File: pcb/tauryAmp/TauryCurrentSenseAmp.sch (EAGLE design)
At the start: 20 parts, among them IC1 AD780R, U1 MAX4239, U2 MAX4239

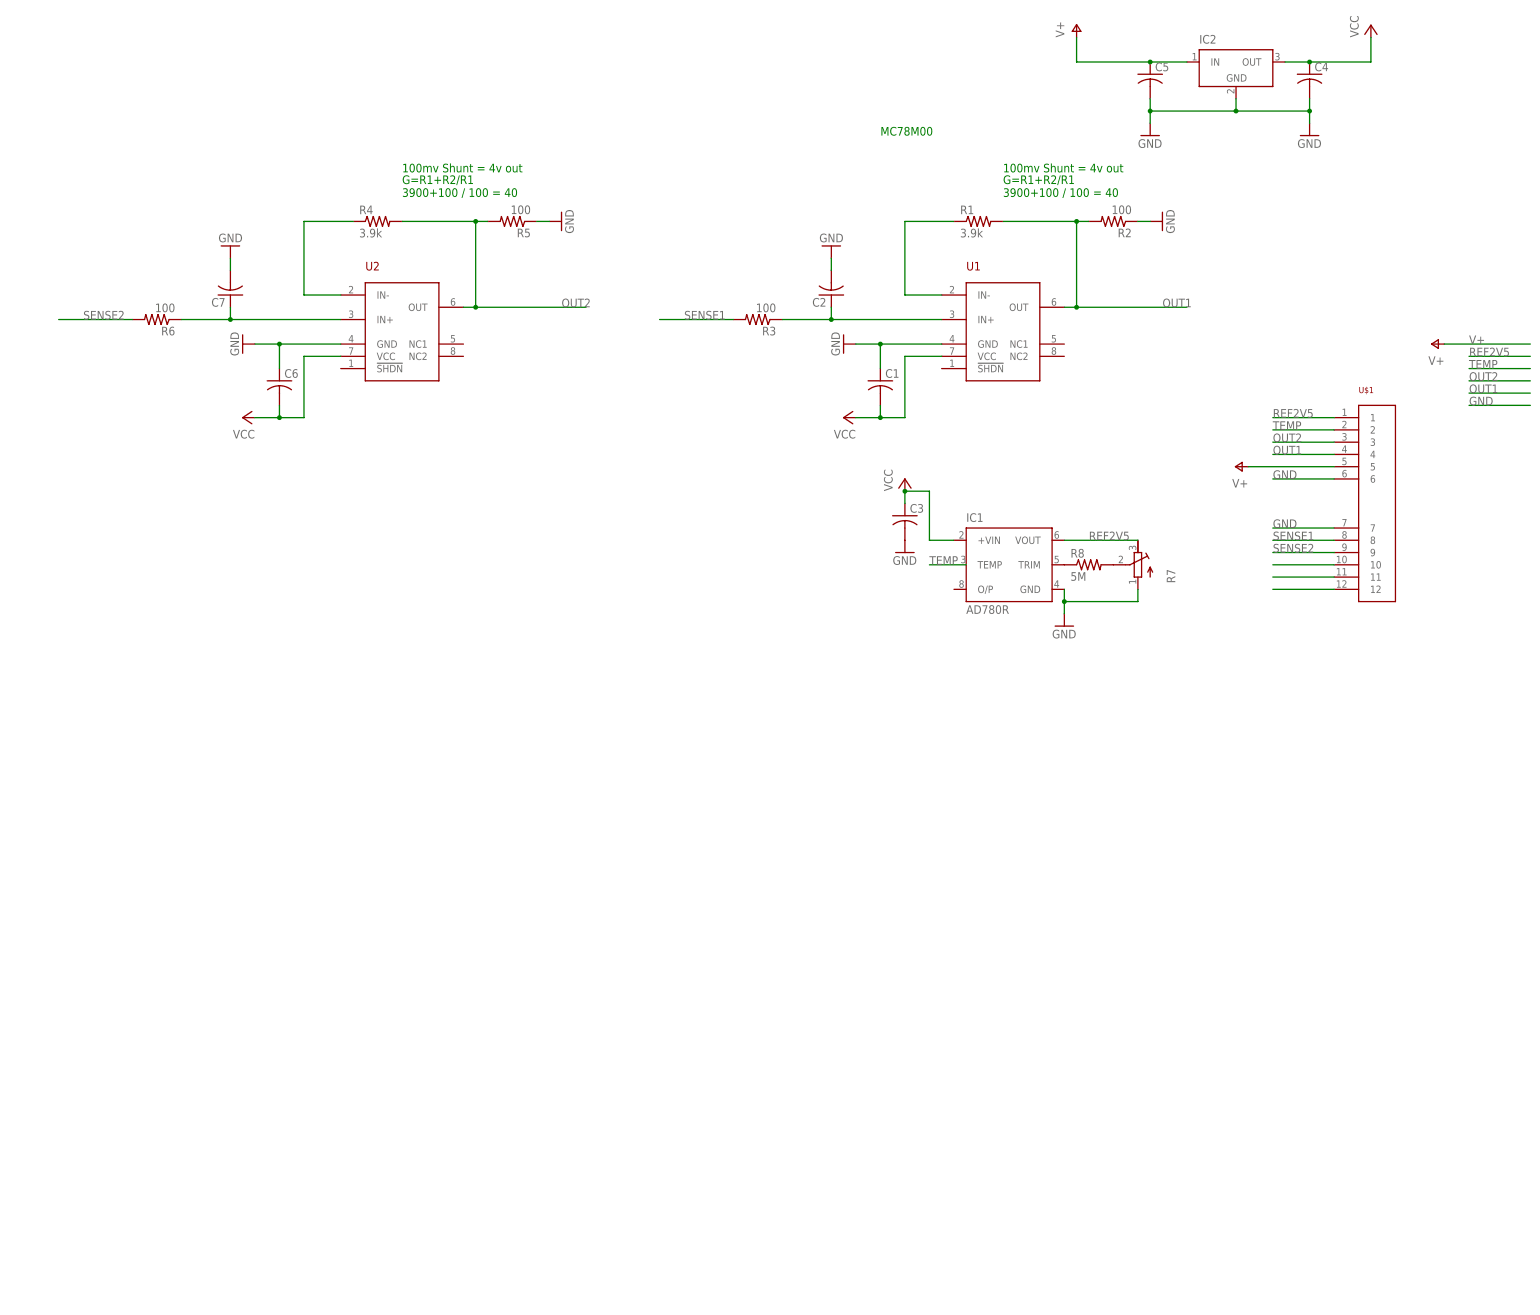
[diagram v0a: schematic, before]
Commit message: improved analog frontend
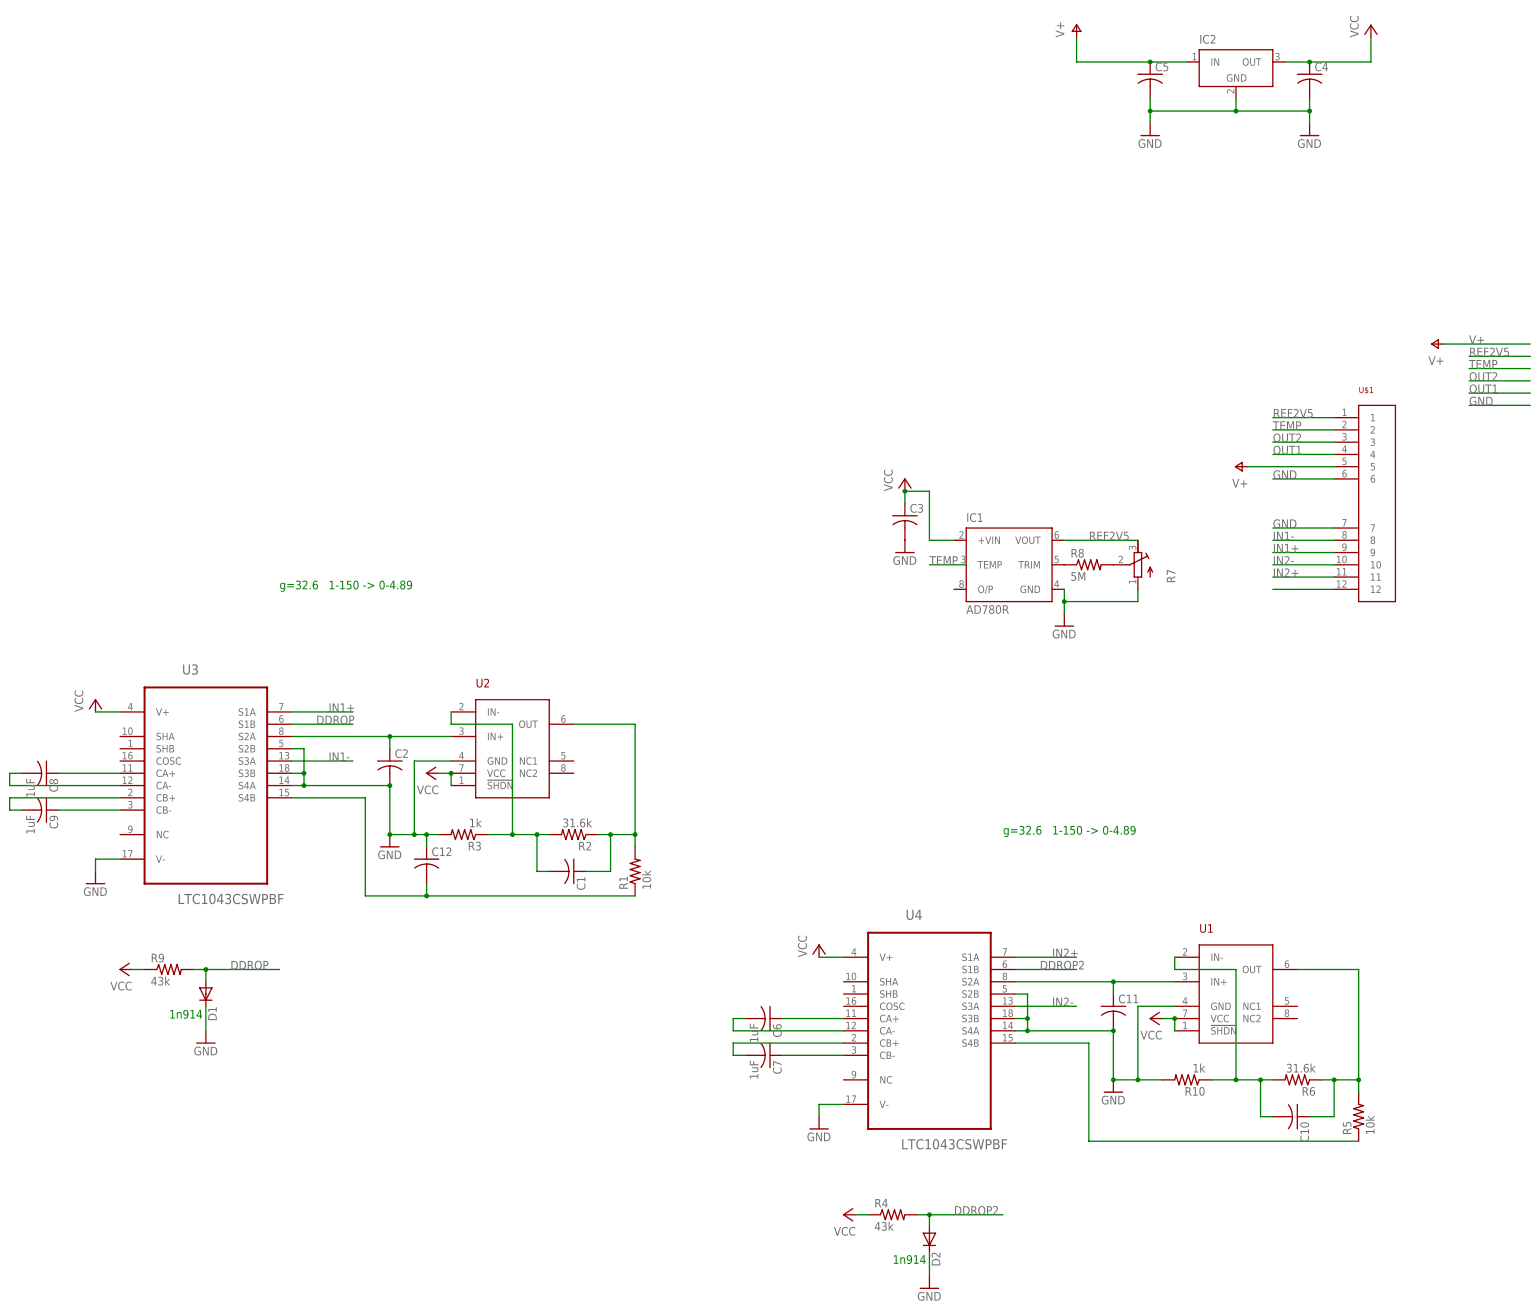
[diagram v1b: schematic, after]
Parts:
- added C10, C11, C12: (no value), rcl:C-USC0805
- added C8, C9: 1uF, rcl:C-USC0805
- added D1: (no value), diode:DIODE-SOD323-R
- added D2: (no value), diode:DIODE-SOD523
- added R10: 1k, rcl:R-US_R0805
- added R9: 43k, rcl:R-US_R0805
- added U3, U4: LTC1043CSWPBF, LTC_By_element14_Batch_1:LTC1043CSWPBF
- C6, C7: value (none) -> 1uF
- R1: value 3.9k -> 10k
- R2, R6: value 100 -> 31.6k
- R3: value 100 -> 1k
- R4: value 3.9k -> 43k
- R5: value 100 -> 10k
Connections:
- removed net N$12: U$1.10
- removed net N$13: U$1.11
- removed net SENSE1: R3.2, U$1.8
- removed net SENSE2: R6.2, U$1.9
- new net DDROP: D1.A, R9.2, U3.S1B
- new net DDROP2: D2.A, R4.2, U4.S1B
- new net IN1+: U$1.9, U3.S1A
- new net IN1-: U$1.8, U3.S3A
- new net IN2+: U$1.11, U4.S1A
- new net IN2-: U$1.10, U4.S3A
- new net N$10: C9.1, U3.CB-
- new net N$15: C6.2, U4.CA-
- new net N$16: C7.2, U4.CB+
- new net N$17: C7.1, U4.CB-
- new net N$18: C11.1, U1.IN+, U4.S2A
- new net N$19: R5.1, U4.S4B
- new net N$20: C10.2, R10.1, R6.2, U1.IN-
- new net N$7: C8.1, U3.CA+
- new net N$8: C8.2, U3.CA-
- new net N$9: C9.2, U3.CB+
- net GND: now also C11.2, C12.1, D1.C, D2.C, R10.2, R3.2, U3.S2B, U3.S3B, U3.S4A, U3.V-, U4.S2B, U4.S3B, U4.S4A, U4.V-; no longer C1.1, C6.1, C7.2, R2.1, R5.1
- net N$1: now also C2.1, U2.IN+, U3.S2A; no longer R4.1, U2.IN-
- net N$2: now also C12.2, U3.S4B; no longer U1.IN-
- net N$3: now also C6.1, U4.CA+; no longer C2.1, R3.1, U1.IN+
- net N$4: now also C1.2, R2.2, R3.1, U2.IN-; no longer C7.1, R6.1, U2.IN+
- net OUT1: now also C1.1, R2.1, U2.OUT; no longer R2.2, U1.OUT
- net OUT2: now also C10.1, R6.1, U1.OUT; no longer R4.2, U2.OUT
- net VCC: now also R4.1, R9.1, U1.!SHDN, U2.!SHDN, U3.V+, U4.V+; no longer C1.2, C6.2
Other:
- note added: "1-150 -> 0-4.89"
- note added: "1n914"
- note added: "g=32.6"
- note removed: "100mv Shunt = 4v out"
- note removed: "G=R1+R2/R1 3900+100 / 100 = 40"
- note removed: "MC78M00"
- moved on the sheet: C1, C2, C6, C7, R1, R2, R3, R4, R5, R6, U1, U2
